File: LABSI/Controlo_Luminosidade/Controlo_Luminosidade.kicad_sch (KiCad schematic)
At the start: 44 parts, among them J1 Barrel_Jack_Switch, J10 Touch Button, J2 Barrel_Jack_Switch, J3 Conn_01x05_Pin, J4 Conn_01x04_Pin, J5 Conn_01x04_Pin, J6 AVR-ISP-6, J7 Conn_01x03_Pin, J8 Conn_01x03_Pin, J9 Conn_01x05_Pin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

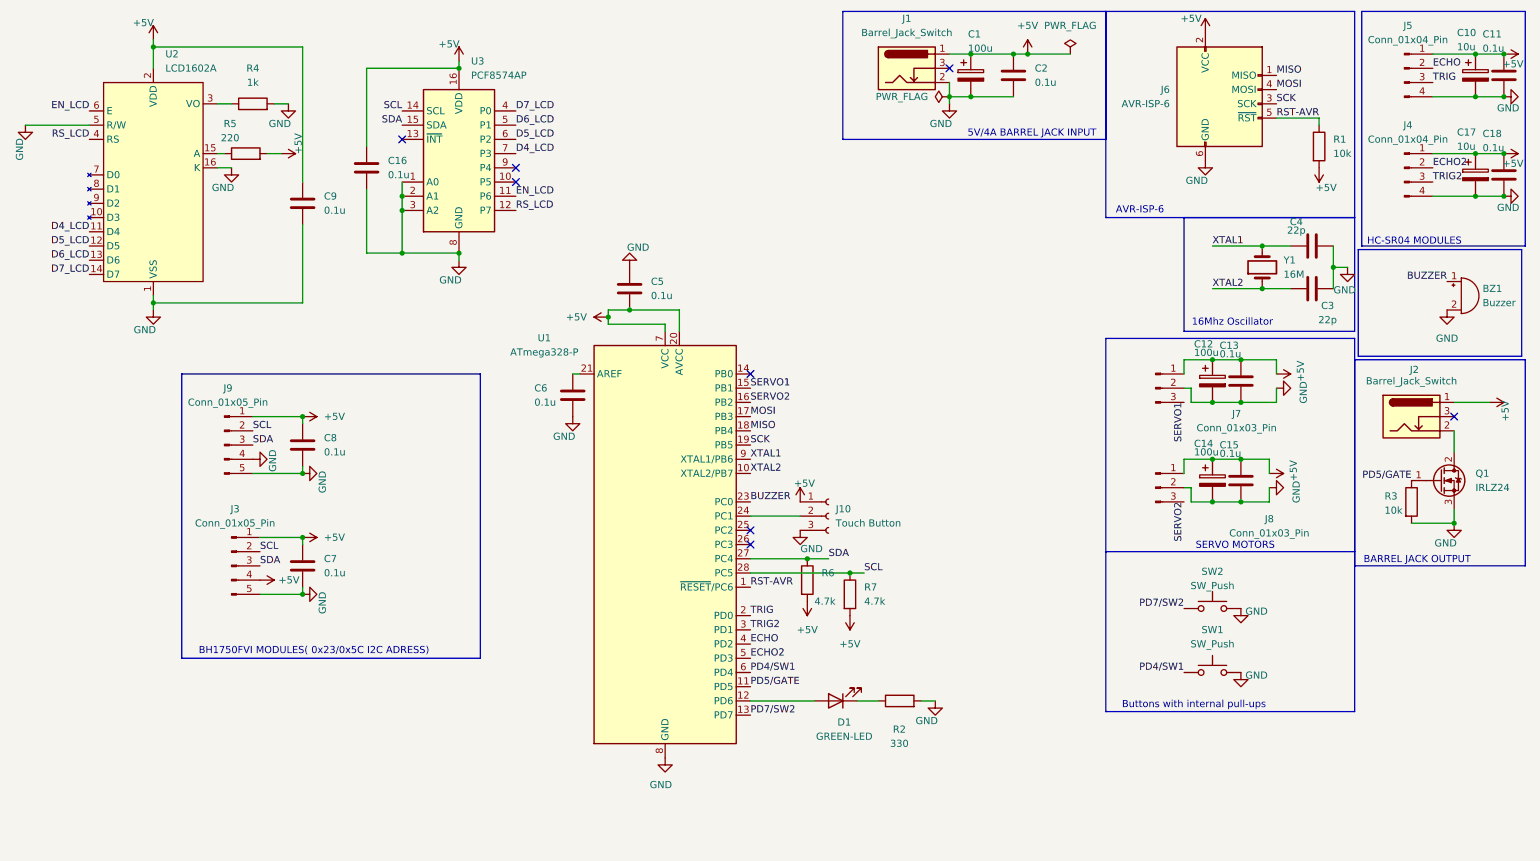
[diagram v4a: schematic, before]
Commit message: botoes touch sem debounce a funcionar, logica motor a funcionar
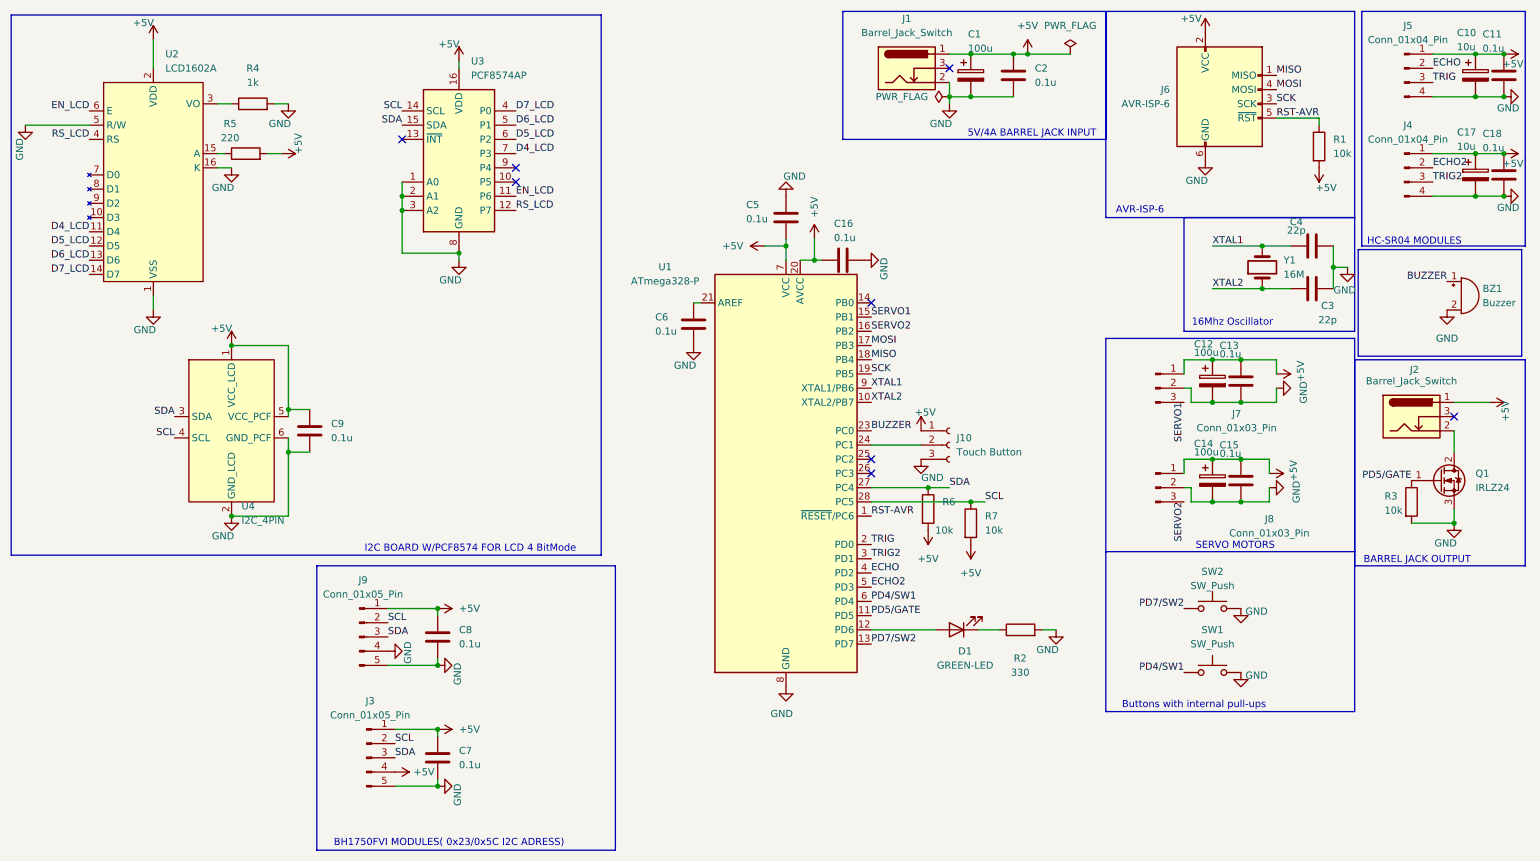
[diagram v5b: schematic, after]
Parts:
- added U4: I2C_4PIN, Connector_PinHeader_2.54mm:PinHeader_2x03_P2.54mm_Vertical, symbol lcd1602A:I2C_PCF8574_4PIN
- BZ1: footprint (none) -> Buzzer_Beeper:Buzzer_12x9.5RM7.6
- R4, R5: footprint Resistor_THT:R_Axial_DIN0204_L3.6mm_D1.6mm_P5.08mm_Horizontal -> (none)
- R6, R7: value 4.7k -> 10k
- SW1, SW2: footprint (none) -> Button_Switch_THT:SW_PUSH_6mm
- U2: footprint Connector_PinSocket_2.54mm:PinSocket_1x16_P2.54mm_Vertical -> (none)
- U3: footprint Package_DIP:DIP-16_W7.62mm -> (none)
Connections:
- net +5V: now also U4.1 (VCC_LCD), U4.5 (VCC_PCF)
- net GND: now also U4.2 (GND_LCD), U4.6 (GND_PCF)
- net SCL: now also U4.4 (SCL)
- net SDA: now also U4.3 (SDA)
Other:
- note added: "I2C BOARD W/PCF8574 FOR LCD 4 BitMode"
- moved on the sheet: C5, C6, C7, C8, C9, D1, J10, J3, J9, R2, R6, R7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

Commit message: att
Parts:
- removed SW1, SW2: SW_Push, Button_Switch_THT:SW_PUSH_6mm, symbol Switch:SW_Push
- added J11, J12: Touch Button, Connector_PinSocket_2.54mm:PinSocket_1x03_P2.54mm_Vertical, symbol Connector:Conn_01x03_Socket
- J4, J5: footprint Connector_PinHeader_2.54mm:PinHeader_1x04_P2.54mm_Vertical -> Connector_PinSocket_2.54mm:PinSocket_1x04_P2.54mm_Vertical
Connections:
- net +5V: now also J11.1 (Pin_1), J12.1 (Pin_1)
- net GND: now also J11.3 (Pin_3), J12.3 (Pin_3)
- net PD4/SW1: now also J12.2 (Pin_2)
- net PD7/SW2: now also J11.2 (Pin_2)
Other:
- note added: "Touch buttons for lux setpoint"
- note removed: "Buttons with internal pull-ups"
